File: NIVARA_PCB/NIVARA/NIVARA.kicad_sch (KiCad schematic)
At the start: 0 parts

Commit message: kicad
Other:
- sheet NIVARA_BOARD ports: added IN_NPN{1,2,Gnd}, IN_PNP{1,2,Gnd}, OP_NPN{1,2,Gnd}, OP_PNP{1,2,Gnd}; removed none
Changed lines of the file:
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@@
 	(paper "A4")
 	(sheet
-		(at 127 72.39)
-		(size 31.75 39.37)
+		(at 111.76 55.88)
+		(size 38.1 39.37)
 		(exclude_from_sim no)
 		(in_bom yes)
@@
 		)
 		(property "Sheetname" "NIVARA_BOARD"
-			(at 127 71.6784 0)
+			(at 111.76 55.1684 0)
 			(effects
 				(font
@@
 		)
 		(property "Sheetfile" "NIVARA_BOARD.kicad_sch"
-			(at 127 112.3446 0)
+			(at 111.76 95.8346 0)
 			(effects
 				(font
@@
 			)
 		)
+		(pin "IN_NPN{1,2,Gnd}" input
+			(at 111.76 59.69 180)
+			(effects
+				(font
+					(size 1.27 1.27)
+				)
+				(justify left)
+			)
+		)
+		(pin "OP_NPN{1,2,Gnd}" output
+			(at 149.86 59.69 0)
+			(effects
+				(font
+					(size 1.27 1.27)
+				)
+				(justify right)
+			)
+		)
+		(pin "IN_PNP{1,2,Gnd}" input
+			(at 111.76 66.04 180)
+			(effects
+				(font
+					(size 1.27 1.27)
+				)
+				(justify left)
+			)
+		)
+		(pin "OP_PNP{1,2,Gnd}" output
+			(at 149.86 66.04 0)
+			(effects
+				(font
+					(size 1.27 1.27)
+				)
+				(justify right)
+			)
+		)

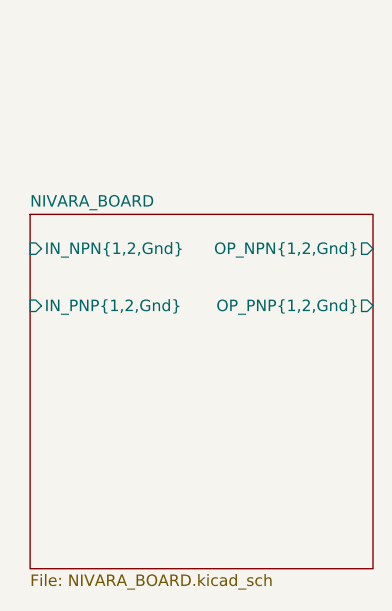
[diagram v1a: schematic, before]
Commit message: AVANCES
se realizaron avances con las entradas NPN, PNP. tambien se realizaron avances con las salidas de RELAYS
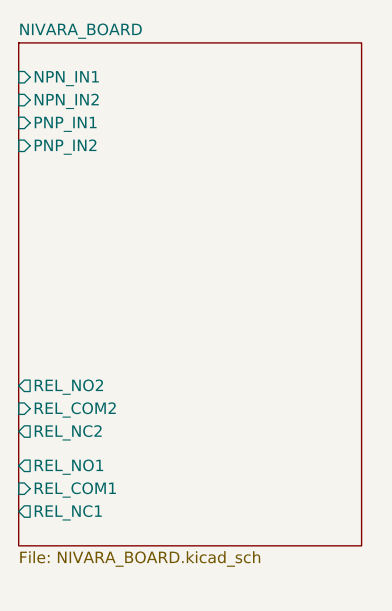
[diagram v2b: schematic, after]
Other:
- sheet NIVARA_BOARD ports: added NPN_IN1, NPN_IN2, PNP_IN1, PNP_IN2, REL_COM1, REL_COM2, REL_NC1, REL_NC2, REL_NO1, REL_NO2; removed IN_NPN{1,2,Gnd}, IN_PNP{1,2,Gnd}, OP_NPN{1,2,Gnd}, OP_PNP{1,2,Gnd}
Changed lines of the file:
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@@
 	(paper "A4")
 	(sheet
-		(at 111.76 55.88)
-		(size 38.1 39.37)
+		(at 110.49 36.83)
+		(size 38.1 55.88)
 		(exclude_from_sim no)
 		(in_bom yes)
@@
 		)
 		(property "Sheetname" "NIVARA_BOARD"
-			(at 111.76 55.1684 0)
+			(at 110.49 36.1184 0)
 			(effects
 				(font
@@
 		)
 		(property "Sheetfile" "NIVARA_BOARD.kicad_sch"
-			(at 111.76 95.8346 0)
+			(at 110.49 93.2946 0)
 			(effects
 				(font
@@
 			)
 		)
-		(pin "IN_NPN{1,2,Gnd}" input
-			(at 111.76 59.69 180)
+		(pin "PNP_IN2" input
+			(at 110.49 48.26 180)
 			(effects
 				(font
@@
 			)
 		)
-		(pin "OP_NPN{1,2,Gnd}" output
-			(at 149.86 59.69 0)
-			(effects
-				(font
-					(size 1.27 1.27)
-				)
-				(justify right)
-			)
-		)
-		(pin "IN_PNP{1,2,Gnd}" input
-			(at 111.76 66.04 180)
+		(pin "PNP_IN1" input
+			(at 110.49 45.72 180)
 			(effects
 				(font
@@
 			)
 		)
-		(pin "OP_PNP{1,2,Gnd}" output
-			(at 149.86 66.04 0)
+		(pin "NPN_IN2" input
+			(at 110.49 43.18 180)
 			(effects
 				(font
 					(size 1.27 1.27)
 				)
-				(justify right)
+				(justify left)
 			)
 		)
+		(pin "NPN_IN1" input
+			(at 110.49 40.64 180)
+			(effects
+				(font
+					(size 1.27 1.27)
+				)
+				(justify left)
+			)
+		)
+		(pin "REL_NC2" output
+			(at 110.49 80.01 180)
+			(effects
+				(font
+					(size 1.27 1.27)
+				)
+				(justify left)
+			)
+		)
+		(pin "REL_NO2" output
+			(at 110.49 74.93 180)
+			(effects
+				(font
+					(size 1.27 1.27)
+				)
+				(justify left)
+			)
+		)
+		(pin "REL_COM2" input
+			(at 110.49 77.47 180)
+			(effects
+				(font
+					(size 1.27 1.27)
+				)
+				(justify left)
+			)
+		)
+		(pin "REL_NC1" output
+			(at 110.49 88.9 180)
+			(effects
+				(font
+					(size 1.27 1.27)
+				)
+				(justify left)
+			)
+		)
+		(pin "REL_NO1" output
+			(at 110.49 83.82 180)
+			(effects
+				(font
+					(size 1.27 1.27)
+				)
+				(justify left)
+			)
+		)
+		(pin "REL_COM1" input
+			(at 110.49 86.36 180)
+			(effects
+				(font
+					(size 1.27 1.27)
+				)
+				(justify left)
+			)
+		)

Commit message: ACTUALIZACION
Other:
- sheet NIVARA_BOARD ports: added RS_A, RS_B; removed none
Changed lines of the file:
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@@
+			)
+		)
+		(pin "RS_B" bidirectional
+			(at 148.59 86.36 0)
+			(effects
+				(font
+					(size 1.27 1.27)
+				)
+				(justify right)
+			)
+		)
+		(pin "RS_A" bidirectional
+			(at 148.59 88.9 0)
+			(effects
+				(font
+					(size 1.27 1.27)
+				)
+				(justify right)
 			)
 		)

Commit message: ACTUALIZACION
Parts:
- added J1: Power, TerminalBlock:TerminalBlock_bornier-2_P5.08mm, symbol Connector:Screw_Terminal_01x02
- added J10: I_ANALOG, symbol Connector:Screw_Terminal_01x04
- added J11: RS485, TerminalBlock:TerminalBlock_bornier-3_P5.08mm, symbol Connector:Screw_Terminal_01x03
- added J12: O_ANALOG, symbol Connector:Screw_Terminal_01x04
- added J3: I_NPN, TerminalBlock:TerminalBlock_bornier-2_P5.08mm, symbol Connector:Screw_Terminal_01x02
- added J4: I_PNP, TerminalBlock:TerminalBlock_bornier-2_P5.08mm, symbol Connector:Screw_Terminal_01x02
- added J5: RELAY_1, TerminalBlock:TerminalBlock_bornier-3_P5.08mm, symbol Connector:Screw_Terminal_01x03
- added J6: RELAY_2, TerminalBlock:TerminalBlock_bornier-3_P5.08mm, symbol Connector:Screw_Terminal_01x03
- added J7: O_NPN, TerminalBlock:TerminalBlock_bornier-2_P5.08mm, symbol Connector:Screw_Terminal_01x02
- added J8: O_PNP, TerminalBlock:TerminalBlock_bornier-2_P5.08mm, symbol Connector:Screw_Terminal_01x02
- added J9: I_DIG, TerminalBlock:TerminalBlock_bornier-2_P5.08mm, symbol Connector:Screw_Terminal_01x02
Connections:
- net NIVARA_BOARD/NPN_IN1: now also J4.1 (Pin_1)
- net NIVARA_BOARD/NPN_IN2: now also J4.2 (Pin_2)
- net NIVARA_BOARD/PNP_IN1: now also J3.1 (Pin_1)
- net NIVARA_BOARD/PNP_IN2: now also J3.2 (Pin_2)
- net NIVARA_BOARD/REL_COM1: now also J6.2 (Pin_2)
- net NIVARA_BOARD/REL_COM2: now also J5.2 (Pin_2)
- net NIVARA_BOARD/REL_NC1: now also J6.1 (Pin_1)
- net NIVARA_BOARD/REL_NC2: now also J5.3 (Pin_3)
- net NIVARA_BOARD/REL_NO1: now also J6.3 (Pin_3)
- net NIVARA_BOARD/REL_NO2: now also J5.1 (Pin_1)
- net NIVARA_BOARD/RS_A: now also J11.2 (Pin_2)
- net NIVARA_BOARD/RS_B: now also J11.1 (Pin_1)
- new net GND: J1.2 (Pin_2), J10.4 (Pin_4), J11.3 (Pin_3), J12.4 (Pin_4)
- new net NIVARA_BOARD/A_IN0_10: J10.1 (Pin_1)
- new net NIVARA_BOARD/A_IN0_32: J10.2 (Pin_2)
- new net NIVARA_BOARD/A_IN4_20: J10.3 (Pin_3)
- new net NIVARA_BOARD/A_OUT0_05: J12.1 (Pin_1)
- new net NIVARA_BOARD/A_OUT0_10: J12.2 (Pin_2)
- new net NIVARA_BOARD/A_OUT4_20: J12.3 (Pin_3)
- new net NIVARA_BOARD/D_IN1: J9.1 (Pin_1)
- new net NIVARA_BOARD/D_IN2: J9.2 (Pin_2)
- new net NIVARA_BOARD/NPN_OUT1: J7.1 (Pin_1)
- new net NIVARA_BOARD/NPN_OUT2: J7.2 (Pin_2)
- new net NIVARA_BOARD/PNP_OUT1: J8.1 (Pin_1)
- new net NIVARA_BOARD/PNP_OUT2: J8.2 (Pin_2)
- new net VCC: J1.1 (Pin_1)
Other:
- sheet NIVARA_BOARD ports: added A_IN0_10, A_IN0_32, A_IN4_20, A_OUT0_05, A_OUT0_10, A_OUT4_20, D_IN1, D_IN2, NPN_OUT1, NPN_OUT2, PNP_OUT1, PNP_OUT2; removed none

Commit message: avance
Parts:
- J10, J12: footprint (none) -> TerminalBlock:TerminalBlock_bornier-4_P5.08mm
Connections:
- net NIVARA_BOARD/REL_NC1: now also J6.3 (Pin_3); no longer J6.1 (Pin_1)
- net NIVARA_BOARD/REL_NO1: now also J6.1 (Pin_1); no longer J6.3 (Pin_3)
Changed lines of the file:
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@@
 			)
 		)
-		(property "Footprint" ""
+		(property "Footprint" "TerminalBlock:TerminalBlock_bornier-4_P5.08mm"
 			(at 102.87 82.55 0)
 			(effects
@@
 			)
 		)
-		(property "Footprint" ""
+		(property "Footprint" "TerminalBlock:TerminalBlock_bornier-4_P5.08mm"
 			(at 156.21 62.23 0)
 			(effects
@@
 		(lib_id "Connector:Screw_Terminal_01x03")
 		(at 156.21 86.36 0)
-		(mirror x)
-		(unit 1)
-		(exclude_from_sim no)
+		(unit 1)
+		(exclude_from_sim no)

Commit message: Se organizaron componentes en el area de PCB
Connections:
- net NIVARA_BOARD/RS_A: now also J11.1 (Pin_1); no longer J11.2 (Pin_2)
- net NIVARA_BOARD/RS_B: now also J11.2 (Pin_2); no longer J11.1 (Pin_1)
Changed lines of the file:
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@@
+	(wire
+		(pts
+			(xy 107.95 68.58) (xy 110.49 68.58)
+		)
+		(stroke
+			(width 0)
+			(type default)
+		)
+	)
 	(wire
 		(pts
@@
 	(wire
 		(pts
-			(xy 110.49 71.12) (xy 107.95 71.12)
-		)
-		(stroke
-			(width 0)
-			(type default)
-		)
-	)
-	(wire
-		(pts
 			(xy 151.13 86.36) (xy 148.59 86.36)
 		)
@@
 	(wire
 		(pts
-			(xy 110.49 68.58) (xy 107.95 68.58)
-		)
-		(stroke
-			(width 0)
-			(type default)
-		)
-	)
-	(wire
-		(pts
 			(xy 151.13 83.82) (xy 148.59 83.82)
 		)
@@
 		(pts
 			(xy 107.95 80.01) (xy 110.49 80.01)
+		)
+		(stroke
+			(width 0)
+			(type default)
+		)
+	)
+	(wire
+		(pts
+			(xy 107.95 71.12) (xy 110.49 71.12)
 		)
 		(stroke
@@
 		)
 		(pin "RS_B" bidirectional
+			(at 110.49 71.12 180)
+			(effects
+				(font
+					(size 1.27 1.27)
+				)
+				(justify left)
+			)
+		)
+		(pin "RS_A" bidirectional
 			(at 110.49 68.58 180)
 			(effects
 				(font
-					(size 1.27 1.27)
-				)
-				(justify left)
-			)
-		)
-		(pin "RS_A" bidirectional
-			(at 110.49 71.12 180)
-			(effects
-				(font

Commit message: organizando componentes en la pcb
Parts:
- J10, J12: PART NUMBERT (none) -> WJ500V-5.08-4P
- J11, J5, J6: PART NUMBERT (none) -> WJ500V-5.08-3P
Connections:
- net GND: now also J12.1 (Pin_1); no longer J12.4 (Pin_4)
- net NIVARA_BOARD/A_OUT0_05: now also J12.4 (Pin_4); no longer J12.1 (Pin_1)
- net NIVARA_BOARD/A_OUT0_10: now also J12.3 (Pin_3); no longer J12.2 (Pin_2)
- net NIVARA_BOARD/A_OUT4_20: now also J12.2 (Pin_2); no longer J12.3 (Pin_3)
- net NIVARA_BOARD/NPN_IN1: now also J3.1 (Pin_1); no longer J4.1 (Pin_1)
- net NIVARA_BOARD/NPN_IN2: now also J3.2 (Pin_2); no longer J4.2 (Pin_2)
- net NIVARA_BOARD/PNP_IN1: now also J4.1 (Pin_1); no longer J3.1 (Pin_1)
- net NIVARA_BOARD/PNP_IN2: now also J4.2 (Pin_2); no longer J3.2 (Pin_2)
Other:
- moved on the sheet: J3, J4
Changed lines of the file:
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@@
 	(generator_version "9.0")
 	(paper "A4")
+	(junction
+		(at 110.49 50.8)
+		(diameter 0)
+		(color 0 0 0 0)
+	)
+	(wire
+		(pts
+			(xy 107.95 53.34) (xy 110.49 53.34)
+		)
+		(stroke
+			(width 0)
+			(type default)
+		)
+	)
 	(wire
 		(pts
@@
 	(wire
 		(pts
+			(xy 107.95 50.8) (xy 110.49 50.8)
+		)
+		(stroke
+			(width 0)
+			(type default)
+		)
+	)
+	(wire
+		(pts
 			(xy 148.59 44.45) (xy 151.13 44.45)
 		)
@@
 	(wire
 		(pts
+			(xy 107.95 44.45) (xy 110.49 44.45)
+		)
+		(stroke
+			(width 0)
+			(type default)
+		)
+	)
+	(wire
+		(pts
 			(xy 31.75 27.94) (xy 31.75 25.4)
 		)
@@
 	(wire
 		(pts
-			(xy 107.95 44.45) (xy 110.49 44.45)
-		)
-		(stroke
-			(width 0)
-			(type default)
-		)
-	)
-	(wire
-		(pts
-			(xy 107.95 53.34) (xy 110.49 53.34)
-		)
-		(stroke
-			(width 0)
-			(type default)
-		)
-	)
-	(wire
-		(pts
 			(xy 151.13 78.74) (xy 148.59 78.74)
 		)
@@
 	(wire
 		(pts
+			(xy 110.49 50.8) (xy 111.76 50.8)
+		)
+		(stroke
+			(width 0)
+			(type default)
+		)
+	)
+	(wire
+		(pts
 			(xy 151.13 88.9) (xy 148.59 88.9)
 		)
@@
 		(pts
 			(xy 107.95 82.55) (xy 110.49 82.55)
-		)
-		(stroke
-			(width 0)
-			(type default)
-		)
-	)
-	(wire
-		(pts
-			(xy 107.95 50.8) (xy 110.49 50.8)
 		)
 		(stroke
@@
 	(symbol
 		(lib_id "Connector:Screw_Terminal_01x02")
-		(at 102.87 41.91 0)
+		(at 102.87 50.8 0)
 		(mirror y)
 		(unit 1)
@@
 		(dnp no)
 		(property "Reference" "J4"
-			(at 97.79 43.18 90)
+			(at 97.79 52.07 90)
 			(effects
 				(font
@@
 		)
 		(property "Value" "I_PNP"
-			(at 100.33 43.18 90)
+			(at 100.33 52.07 90)
 			(effects
 				(font
@@
 		)
 		(property "Footprint" "TerminalBlock:TerminalBlock_bornier-2_P5.08mm"
-			(at 102.87 41.91 0)
+			(at 102.87 50.8 0)
 			(effects
 				(font
@@
 		)
 		(property "Datasheet" "~"
-			(at 102.87 41.91 0)
+			(at 102.87 50.8 0)
 			(effects
 				(font
@@
 		)
 		(property "Description" "Generic screw terminal, single row, 01x02, script generated (kicad-library-utils/schlib/autogen/connector/)"
-			(at 102.87 41.91 0)
+			(at 102.87 50.8 0)
 			(effects
 				(font
@@
 		)
 		(property "PART NUMBERT" "WJ500V-5.08-2P"
-			(at 102.87 41.91 0)
+			(at 102.87 50.8 0)
 			(effects
 				(font
@@
 			)
 		)
+		(property "PART NUMBERT" "WJ500V-5.08-4P"
+			(at 102.87 82.55 0)
+			(effects
+				(font
+					(size 1.27 1.27)
+				)
+				(hide yes)
+			)
+		)
 		(pin "4"
 		)
@@
 	(symbol
 		(lib_id "Connector:Screw_Terminal_01x04")
-		(at 156.21 62.23 0)
+		(at 156.21 64.77 0)
+		(mirror x)
 		(unit 1)
 		(exclude_from_sim no)
@@
 		(dnp no)
 		(property "Reference" "J12"
-			(at 161.29 64.77 90)
+			(at 161.29 62.23 90)
 			(effects
 				(font
@@
 		)
 		(property "Value" "O_ANALOG"
-			(at 158.75 68.58 90)
+			(at 158.75 58.42 90)
 			(effects
 				(font
@@
 		)
 		(property "Footprint" "TerminalBlock:TerminalBlock_bornier-4_P5.08mm"
-			(at 156.21 62.23 0)
+			(at 156.21 64.77 0)
 			(effects
 				(font
@@
 		)
 		(property "Datasheet" "~"
-			(at 156.21 62.23 0)
+			(at 156.21 64.77 0)
 			(effects
 				(font
@@
 		)
 		(property "Description" "Generic screw terminal, single row, 01x04, script generated (kicad-library-utils/schlib/autogen/connector/)"
-			(at 156.21 62.23 0)
+			(at 156.21 64.77 0)
+			(effects
+				(font
+					(size 1.27 1.27)
+				)
+				(hide yes)
+			)
+		)
+		(property "PART NUMBERT" "WJ500V-5.08-4P"
+			(at 156.21 64.77 0)
 			(effects
 				(font
@@
 			)
 		)
+		(property "PART NUMBERT" "WJ500V-5.08-3P"
+			(at 102.87 71.12 0)
+			(effects
+				(font
+					(size 1.27 1.27)
+				)
+				(hide yes)
+			)
+		)
 		(pin "2"
 		)
@@
 	(symbol
 		(lib_id "Connector:Screw_Terminal_01x02")
-		(at 102.87 50.8 0)
+		(at 102.87 41.91 0)
 		(mirror y)
 		(unit 1)
@@
 		(dnp no)
 		(property "Reference" "J3"
-			(at 97.79 52.07 90)
+			(at 97.79 43.18 90)
 			(effects
 				(font
@@
 		)
 		(property "Value" "I_NPN"
-			(at 100.33 52.07 90)
+			(at 100.33 43.18 90)
 			(effects
 				(font
@@
 		)
 		(property "Footprint" "TerminalBlock:TerminalBlock_bornier-2_P5.08mm"
-			(at 102.87 50.8 0)
+			(at 102.87 41.91 0)
 			(effects
 				(font
@@
 		)
 		(property "Datasheet" "~"
-			(at 102.87 50.8 0)
+			(at 102.87 41.91 0)
 			(effects
 				(font
@@
 		)
 		(property "Description" "Generic screw terminal, single row, 01x02, script generated (kicad-library-utils/schlib/autogen/connector/)"
-			(at 102.87 50.8 0)
+			(at 102.87 41.91 0)
 			(effects
 				(font
@@
 		)
 		(property "PART NUMBERT" "WJ500V-5.08-2P"
-			(at 102.87 50.8 0)
+			(at 102.87 41.91 0)
 			(effects
 				(font
@@
 		)
 		(property "Description" "Generic screw terminal, single row, 01x03, script generated (kicad-library-utils/schlib/autogen/connector/)"
+			(at 156.21 86.36 0)
+			(effects
+				(font
+					(size 1.27 1.27)
+				)
+				(hide yes)
+			)
+		)
+		(property "PART NUMBERT" "WJ500V-5.08-3P"
 			(at 156.21 86.36 0)
 			(effects
@@
 			(at 156.21 76.2 0)
 			(effects
+				(font
+					(size 1.27 1.27)
+				)
+				(hide yes)
+			)
+		)
+		(property "PART NUMBERT" "WJ500V-5.08-3P"
+			(at 156.21 76.2 0)
+			(effects

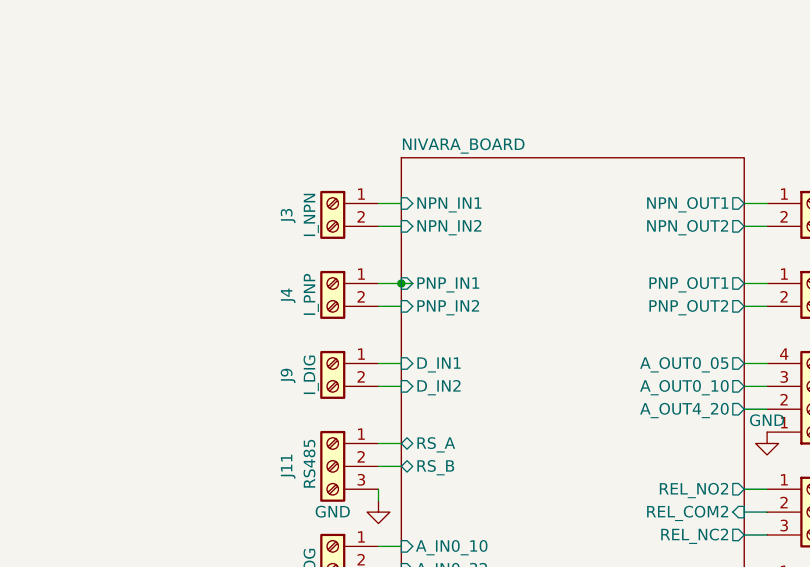
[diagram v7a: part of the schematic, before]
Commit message: arreglo del desastre que tenia con las salidas PNP
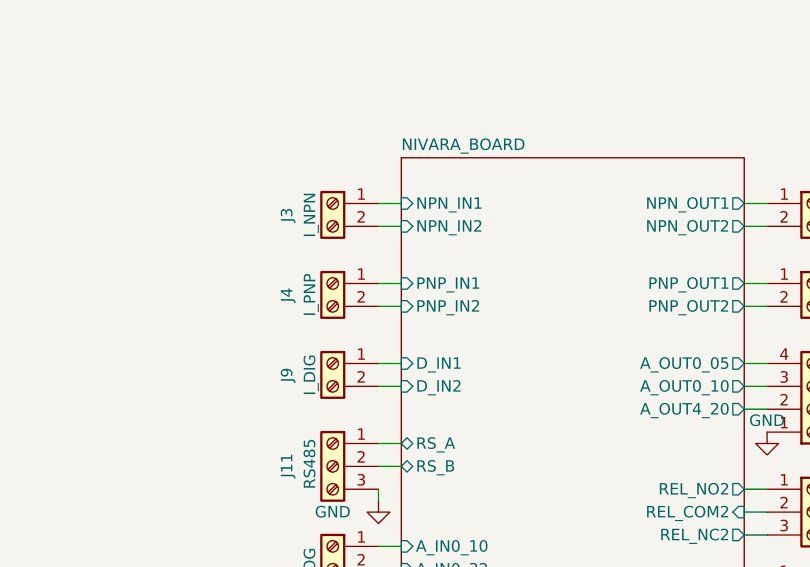
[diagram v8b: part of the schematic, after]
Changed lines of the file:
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@@
 	(generator_version "9.0")
 	(paper "A4")
-	(junction
-		(at 110.49 50.8)
-		(diameter 0)
-		(color 0 0 0 0)
-	)
 	(wire
 		(pts
@@
 		)
 		(stroke
-			(width 0)
-			(type default)
-		)
-	)
-	(wire
-		(pts
-			(xy 110.49 50.8) (xy 111.76 50.8)
-		)
-		(stroke
